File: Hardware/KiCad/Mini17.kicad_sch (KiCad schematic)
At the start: 0 parts

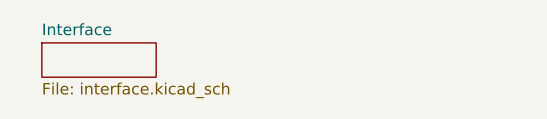
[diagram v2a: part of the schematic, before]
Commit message: Connected SD card to the micro
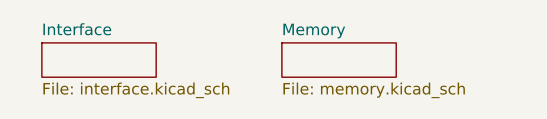
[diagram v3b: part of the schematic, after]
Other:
- added sheet Memory (memory.kicad_sch)
